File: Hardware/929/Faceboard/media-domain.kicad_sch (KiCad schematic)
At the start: 10 parts, among them P7 202-SMART-CAM, U19 TXS0104, U20 TXS0104, U21 TXS0104

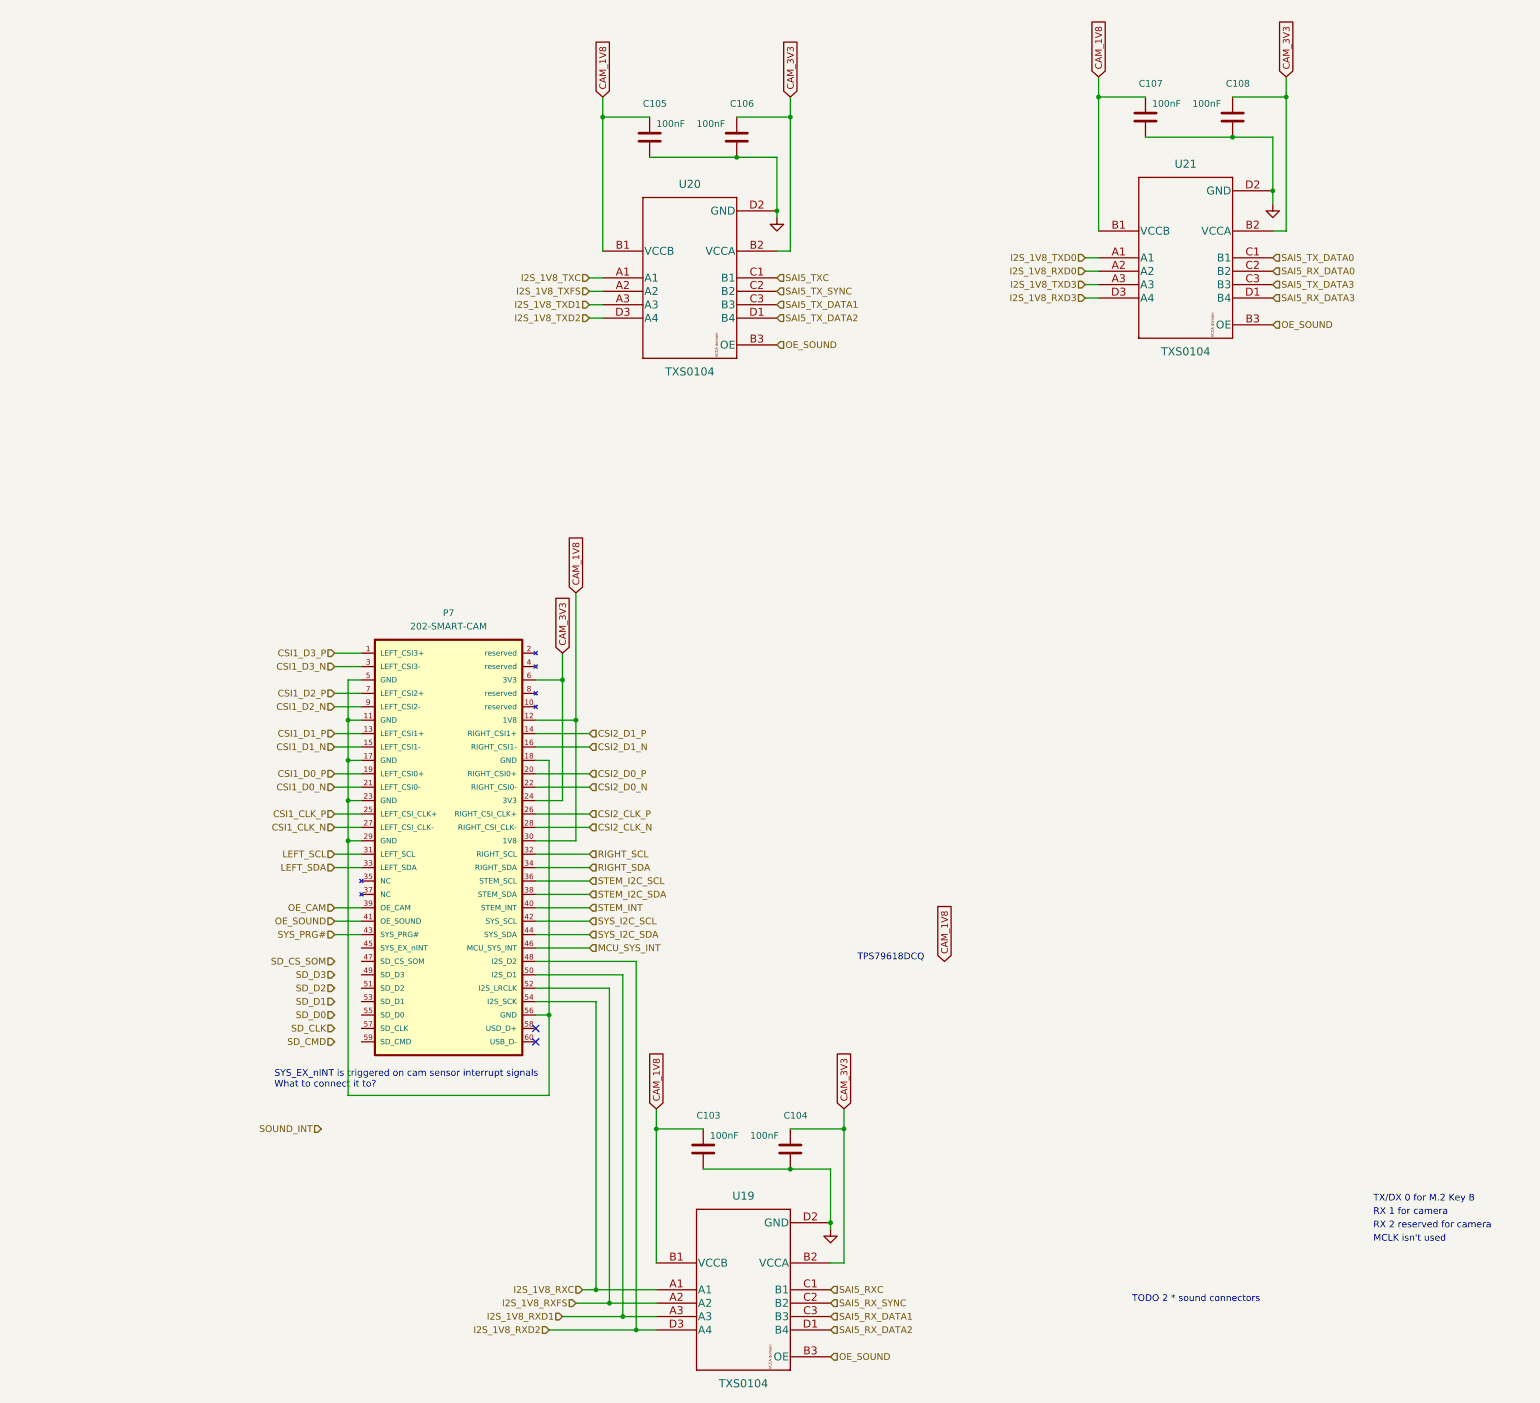
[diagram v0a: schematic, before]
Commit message: Added components
ESD HDMI
Extra components planned
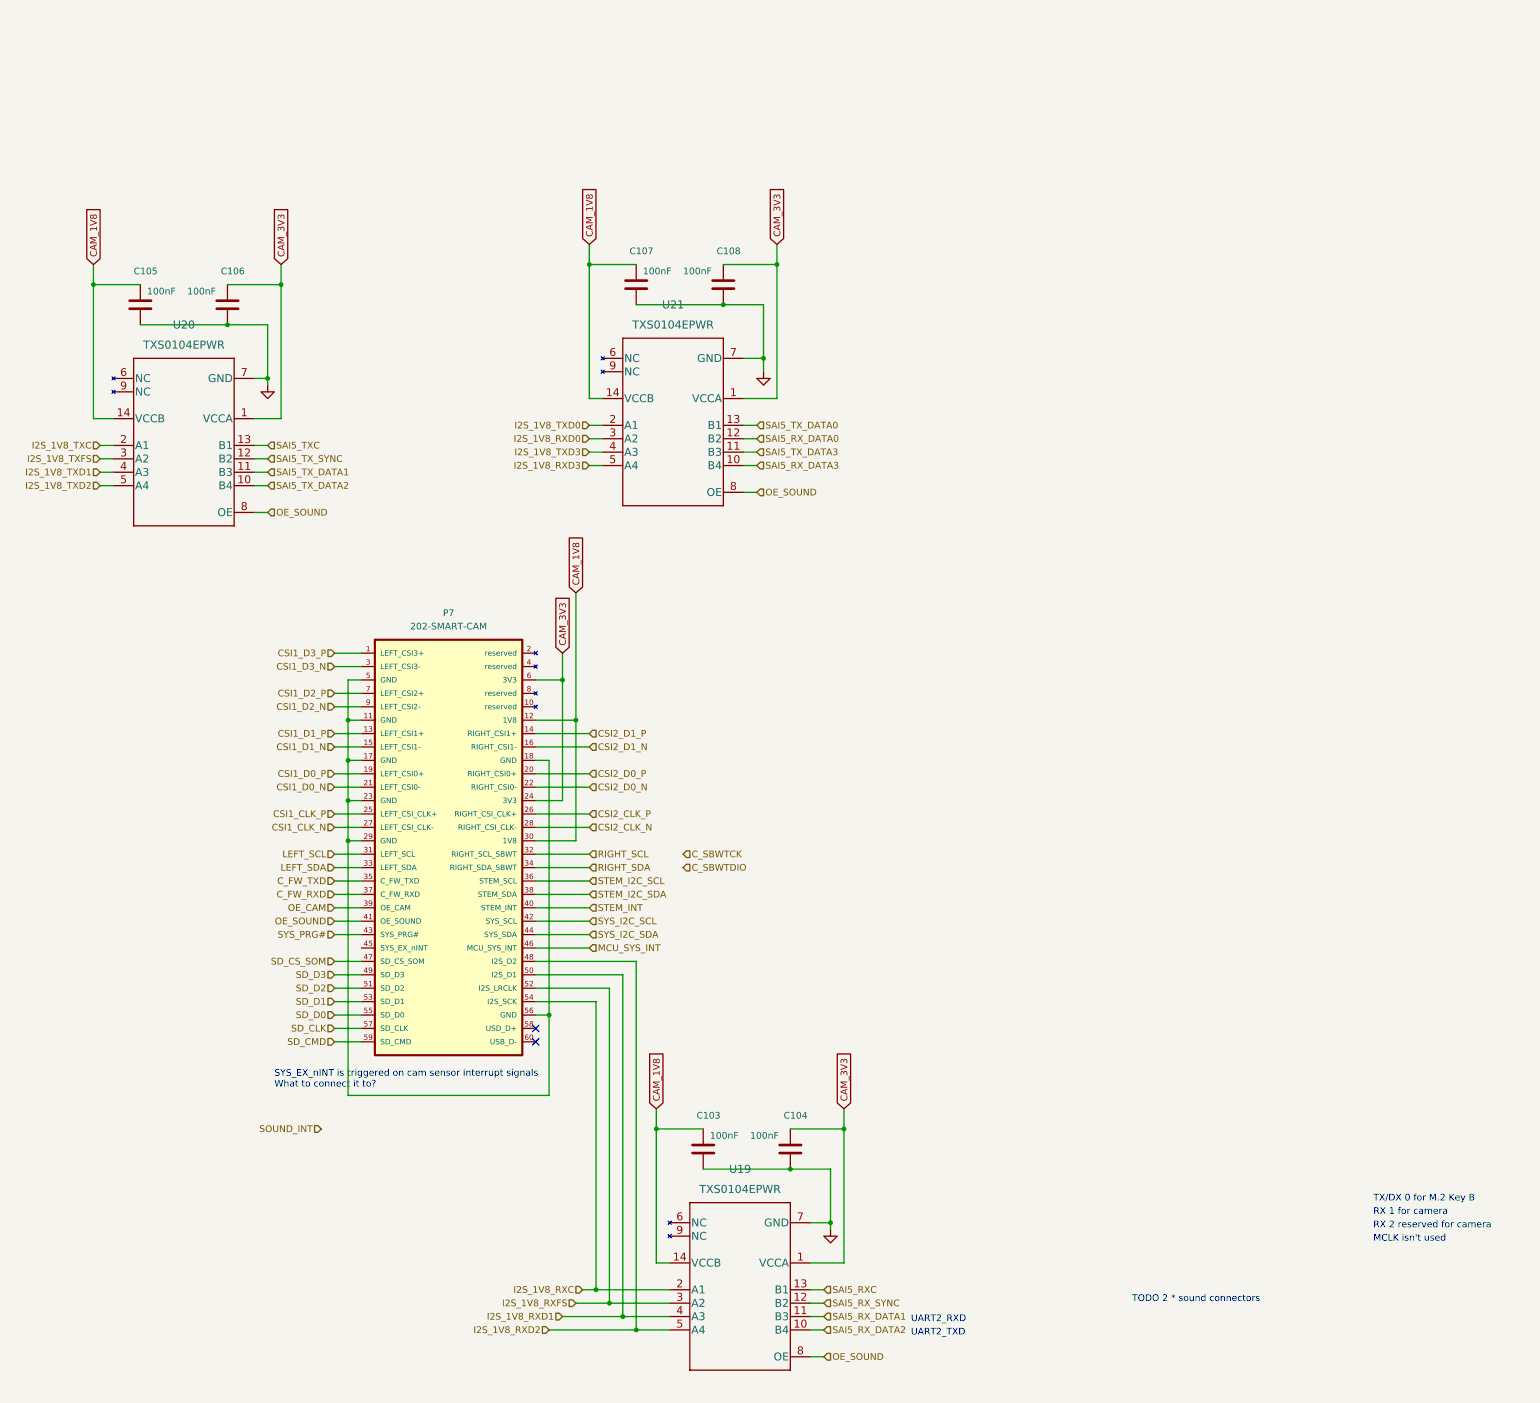
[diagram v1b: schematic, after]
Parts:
- removed U19, U20, U21: TXS0104, Ziloo:TXS0104EYZTR, symbol Ziloo:TXS0104EYZTR
- added U19, U20, U21: TXS0104EPWR, Ziloo:TXS0104EPWR, symbol Ziloo:TXS0104EPWR
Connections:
- net CAM_1V8: now also U19.14 (VCCB), U20.14 (VCCB), U21.14 (VCCB)
- net CAM_3V3: now also U19.1 (VCCA), U20.1 (VCCA), U21.1 (VCCA)
- net GND: now also U19.7 (GND), U20.7 (GND), U21.7 (GND)
- net I2S_1V8_RXC: now also U19.2 (A1)
- net I2S_1V8_RXD0: now also U21.3 (A2)
- net I2S_1V8_RXD1: now also U19.4 (A3)
- net I2S_1V8_RXD2: now also U19.5 (A4)
- net I2S_1V8_RXD3: now also U21.5 (A4)
- net I2S_1V8_RXFS: now also U19.3 (A2)
- net I2S_1V8_TXC: now also U20.2 (A1)
- net I2S_1V8_TXD0: now also U21.2 (A1)
- net I2S_1V8_TXD1: now also U20.4 (A3)
- net I2S_1V8_TXD2: now also U20.5 (A4)
- net I2S_1V8_TXD3: now also U21.4 (A3)
- net I2S_1V8_TXFS: now also U20.3 (A2)
- net OE_SOUND: now also U19.8 (OE), U20.8 (OE), U21.8 (OE)
- net SAI5_RXC: now also U19.13 (B1)
- net SAI5_RX_DATA0: now also U21.12 (B2)
- net SAI5_RX_DATA1: now also U19.11 (B3)
- net SAI5_RX_DATA2: now also U19.10 (B4)
- net SAI5_RX_DATA3: now also U21.10 (B4)
- net SAI5_RX_SYNC: now also U19.12 (B2)
- net SAI5_TXC: now also U20.13 (B1)
- net SAI5_TX_DATA0: now also U21.13 (B1)
- net SAI5_TX_DATA1: now also U20.11 (B3)
- net SAI5_TX_DATA2: now also U20.10 (B4)
- net SAI5_TX_DATA3: now also U21.11 (B3)
- net SAI5_TX_SYNC: now also U20.12 (B2)
- net SD_CLK: now also P7.57 (SD_CLK)
- net SD_CMD: now also P7.59 (SD_CMD)
- net SD_CS_SOM: now also P7.47 (SD_CS_SOM)
- net SD_D0: now also P7.55 (SD_D0)
- net SD_D1: now also P7.53 (SD_D1)
- net SD_D2: now also P7.51 (SD_D2)
- net SD_D3: now also P7.49 (SD_D3)
- net C_FW_TXD: now reaches P7.35 (C_FW_TXD)
- net C_FW_RXD: now reaches P7.37 (C_FW_RXD)
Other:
- note added: "UART2_RXD"
- note added: "UART2_TXD"
- note removed: "TPS79618DCQ"
- moved on the sheet: C105, C106, C107, C108

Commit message: Removed VSOM diodes
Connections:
- net RIGHT_SCL is gone; now on net C_SBWTCK: P7.32 (RIGHT_SCL_SBWT)
- net RIGHT_SDA is gone; now on net C_SBWTDIO: P7.34 (RIGHT_SDA_SBWT)
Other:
- note added: "These can be combined to a TXS0108EPWR"
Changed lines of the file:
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@@
   (junction (at 265.43 64.77) (diameter 0) (color 0 0 0 0)
   )
+  (junction (at 247.65 176.53) (diameter 0) (color 0 0 0 0)
+  )
   (junction (at 233.68 261.62) (diameter 0) (color 0 0 0 0)
   )
@@
   )
   (junction (at 184.15 151.13) (diameter 0) (color 0 0 0 0)
+  )
+  (junction (at 247.65 179.07) (diameter 0) (color 0 0 0 0)
   )
   (junction (at 236.22 264.16) (diameter 0) (color 0 0 0 0)
@@
     (stroke (width 0) (type default) (color 0 0 0 0))
   )
-  (wire (pts (xy 219.71 186.69) (xy 229.87 186.69))
+  (wire (pts (xy 219.71 186.69) (xy 238.76 186.69))
     (stroke (width 0) (type default) (color 0 0 0 0))
   )
@@
     (stroke (width 0) (type default) (color 0 0 0 0))
   )
+  (wire (pts (xy 250.19 173.99) (xy 247.65 173.99))
+    (stroke (width 0) (type default) (color 0 0 0 0))
+  )
   (wire (pts (xy 181.61 176.53) (xy 186.69 176.53))
     (stroke (width 0) (type default) (color 0 0 0 0))
@@
     (stroke (width 0) (type default) (color 0 0 0 0))
   )
+  (wire (pts (xy 247.65 179.07) (xy 250.19 179.07))
+    (stroke (width 0) (type default) (color 0 0 0 0))
+  )
   (wire (pts (xy 274.32 264.16) (xy 271.78 264.16))
     (stroke (width 0) (type default) (color 0 0 0 0))
@@
     (stroke (width 0) (type default) (color 0 0 0 0))
   )
+  (wire (pts (xy 247.65 176.53) (xy 250.19 176.53))
+    (stroke (width 0) (type default) (color 0 0 0 0))
+  )
   (wire (pts (xy 222.25 158.75) (xy 222.25 207.01))
     (stroke (width 0) (type default) (color 0 0 0 0))
@@
     (stroke (width 0) (type default) (color 0 0 0 0))
   )
+  (wire (pts (xy 250.19 181.61) (xy 247.65 181.61))
+    (stroke (width 0) (type default) (color 0 0 0 0))
+  )
   (wire (pts (xy 184.15 166.37) (xy 184.15 158.75))
     (stroke (width 0) (type default) (color 0 0 0 0))
@@
     (stroke (width 0) (type default) (color 0 0 0 0))
   )
+  (wire (pts (xy 247.65 181.61) (xy 247.65 179.07))
+    (stroke (width 0) (type default) (color 0 0 0 0))
+  )
   (wire (pts (xy 219.71 173.99) (xy 227.33 173.99))
     (stroke (width 0) (type default) (color 0 0 0 0))
@@
     (stroke (width 0) (type default) (color 0 0 0 0))
   )
-  (wire (pts (xy 219.71 176.53) (xy 229.87 176.53))
+  (wire (pts (xy 219.71 176.53) (xy 247.65 176.53))
     (stroke (width 0) (type default) (color 0 0 0 0))
   )
@@
     (stroke (width 0) (type default) (color 0 0 0 0))
   )
-  (wire (pts (xy 219.71 179.07) (xy 229.87 179.07))
+  (wire (pts (xy 219.71 179.07) (xy 247.65 179.07))
     (stroke (width 0) (type default) (color 0 0 0 0))
   )
   (wire (pts (xy 181.61 201.93) (xy 186.69 201.93))
+    (stroke (width 0) (type default) (color 0 0 0 0))
+  )
+  (wire (pts (xy 247.65 173.99) (xy 247.65 176.53))
     (stroke (width 0) (type default) (color 0 0 0 0))
   )
@@
     (effects (font (size 1.27 1.27)) (justify left bottom))
   )
+  (text "These can be combined to \na TXS0108EPWR" (at 190.5 72.39 0)
+    (effects (font (size 1.27 1.27)) (justify left bottom))
+  )
   (text "TX/DX 0 for M.2 Key B" (at 378.46 242.57 0)
     (effects (font (size 1.27 1.27)) (justify left bottom))
@@
   )
   (text "UART2_TXD\n" (at 290.83 267.97 0)
+    (effects (font (size 1.27 1.27)) (justify left bottom))
+  )
+  (label "STEM_MSG" (at 223.52 186.69 0)
     (effects (font (size 1.27 1.27)) (justify left bottom))
   )
@@
     (effects (font (size 1.27 1.27)) (justify right))
   )
-  (hierarchical_label "C_SBWTDIO" (shape input) (at 247.65 179.07 0)
+  (hierarchical_label "C_SBWTDIO" (shape input) (at 250.19 181.61 0)
     (effects (font (size 1.27 1.27)) (justify left))
   )
@@
     (effects (font (size 1.27 1.27)) (justify left))
   )
-  (hierarchical_label "RIGHT_SDA" (shape input) (at 229.87 179.07 0)
+  (hierarchical_label "RIGHT_SDA" (shape input) (at 250.19 179.07 0)
     (effects (font (size 1.27 1.27)) (justify left))
   )
@@
     (effects (font (size 1.27 1.27)) (justify right))
   )
-  (hierarchical_label "STEM_INT" (shape input) (at 229.87 186.69 0)
+  (hierarchical_label "STEM_INT" (shape input) (at 238.76 186.69 0)
     (effects (font (size 1.27 1.27)) (justify left))
   )
@@
     (effects (font (size 1.27 1.27)) (justify right))
   )
-  (hierarchical_label "RIGHT_SCL" (shape input) (at 229.87 176.53 0)
+  (hierarchical_label "RIGHT_SCL" (shape input) (at 250.19 176.53 0)
     (effects (font (size 1.27 1.27)) (justify left))
   )
@@
     (effects (font (size 1.27 1.27)) (justify right))
   )
-  (hierarchical_label "C_SBWTCK" (shape input) (at 247.65 176.53 0)
-    (effects (font (size 1.27 1.27)) (justify left))
-  )
+  (hierarchical_label "C_SBWTCK" (shape input) (at 250.19 173.99 0)
+    (effects (font (size 1.27 1.27)) (justify left))
+  )

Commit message: PoC board task
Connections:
- net STEM_INT renamed STEM_MSG
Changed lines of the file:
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@@
     (effects (font (size 1.27 1.27)) (justify right))
   )
-  (hierarchical_label "STEM_INT" (shape input) (at 238.76 186.69 0)
+  (hierarchical_label "STEM_MSG" (shape input) (at 238.76 186.69 0)
     (effects (font (size 1.27 1.27)) (justify left))
   )
